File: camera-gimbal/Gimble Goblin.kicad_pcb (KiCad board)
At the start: 2 copper layers, 44.5 x 36.6 mm, 33 parts, among them J1 Conn_02x03_Odd_Even, J2 Conn_01x03_Male, J3 Conn_01x03_Male, J4 Conn_01x03_Male, J5 PROG, SW1 SW_Push, U1 L7805, U2 MCP2515-EST, U3 ATA6560,1, U4 L7805, U5 ATmega328P-AU, Y1 20MHz, Y2 16MHz

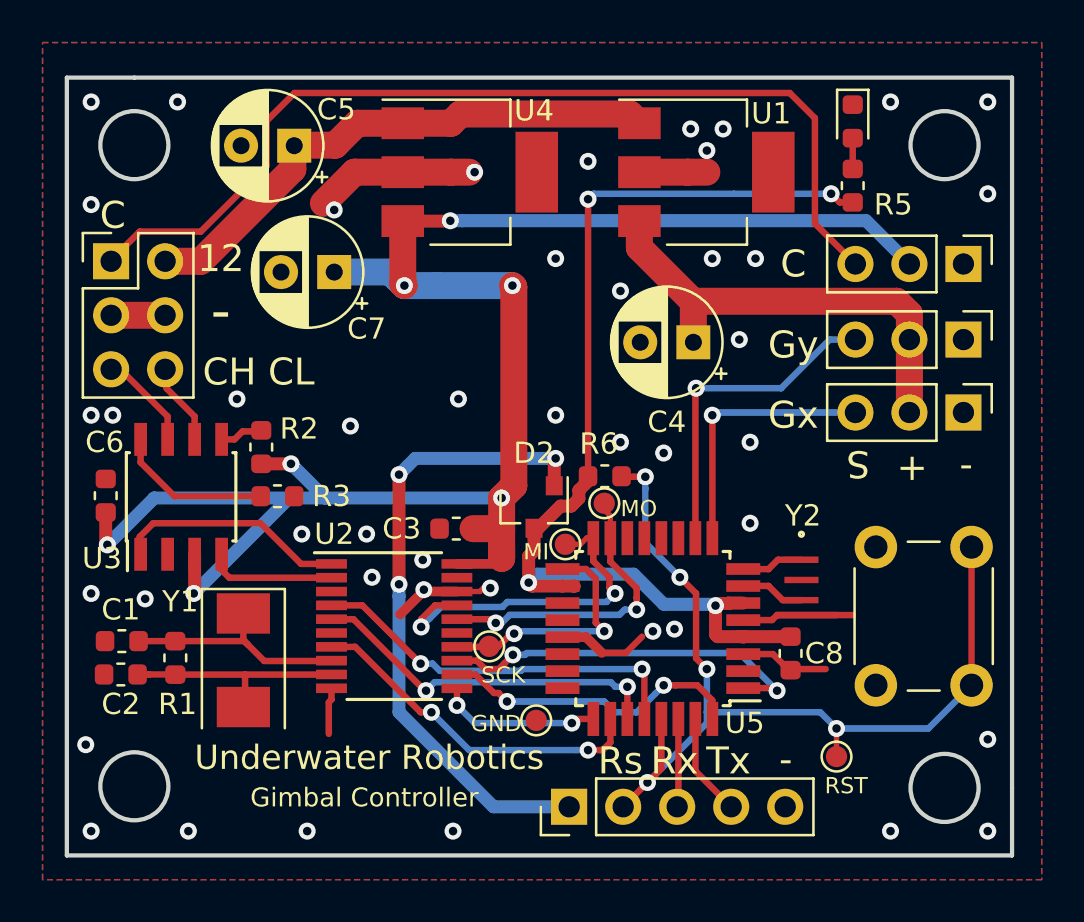
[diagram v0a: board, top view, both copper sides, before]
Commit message: Replaced moutning holes drawn in edge cuts with real holes and regenerated all gerbers
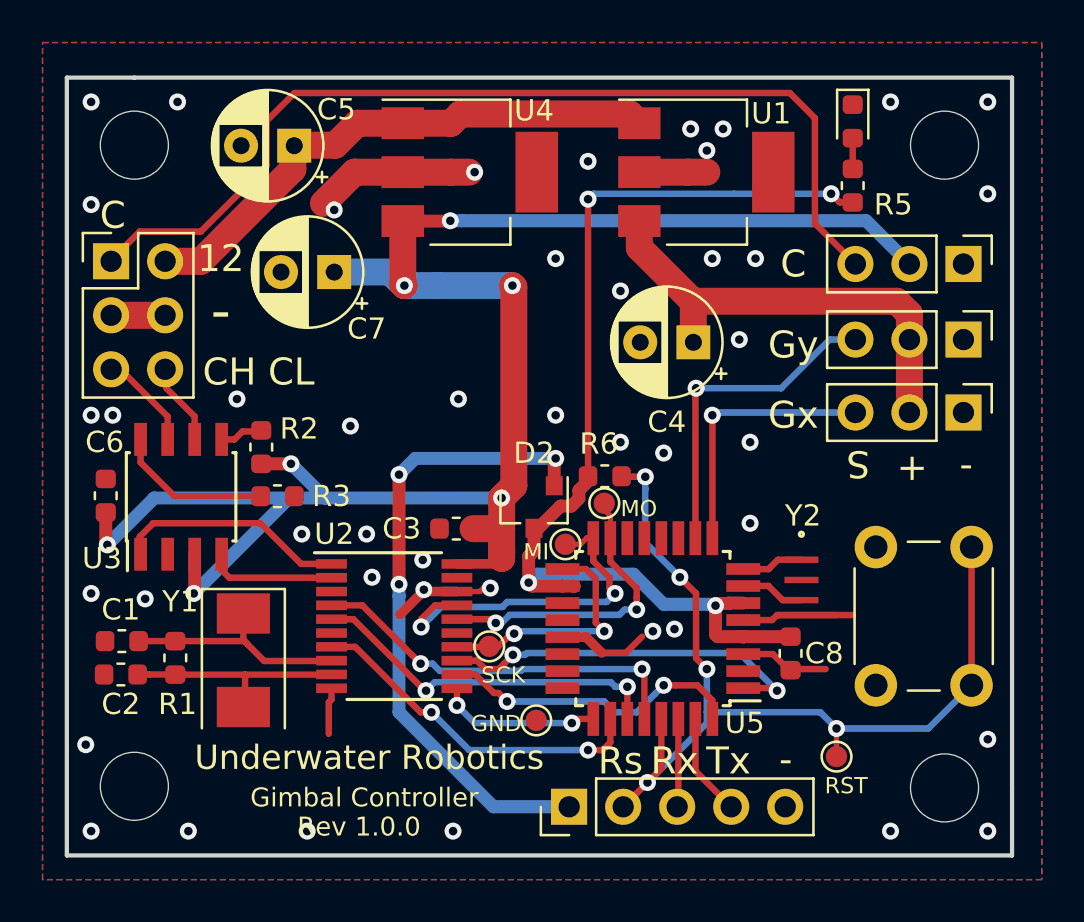
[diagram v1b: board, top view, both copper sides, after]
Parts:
- added REF**: MountingHole_3.2mm_M3, MountingHole:MountingHole_3.2mm_M3, F.Cu at (111.0, 98.5)
- added REF**: MountingHole_3.2mm_M3, MountingHole:MountingHole_3.2mm_M3, F.Cu at (149.1, 98.6)
- added REF**: MountingHole_3.2mm_M3, MountingHole:MountingHole_3.2mm_M3, F.Cu at (149.1, 68.3)
- added REF**: MountingHole_3.2mm_M3, MountingHole:MountingHole_3.2mm_M3, F.Cu at (111.0, 68.3)
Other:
- outline, holes or cut-outs redrawn
- board text added: "Rev 1.0.0"
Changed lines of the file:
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@@
   (general
     (thickness 1.6)
-    (drawings 31)
+    (drawings 28)
     (tracks 393)
     (zones 0)
-    (modules 33)
+    (modules 37)
     (nets 47)
   )
@@
       (drillshape 0)
       (scaleselection 1)
-      (outputdirectory "gerbers_drills/"))
+      (outputdirectory "C:/Users/User/Documents/GitHub/TITAN-Electrical/camera-gimbal/"))
   )
   (net 0 "")
@@
     (add_net VPP)
     (add_net V_MCU)
+  )
+  (module MountingHole:MountingHole_3.2mm_M3 (layer F.Cu)
+    (at 110.998 98.4758)
+    (descr "Mounting Hole 3.2mm, no annular, M3")
+    (tags "mounting hole 3.2mm no annular m3")
+    (attr virtual)
+    (fp_text reference REF** (at 0 -4.2) (layer F.SilkS) hide
+      (effects (font (size 1 1) (thickness 0.15)))
+    )
+    (fp_text value MountingHole_3.2mm_M3 (at 0 4.2) (layer F.Fab)
+      (effects (font (size 1 1) (thickness 0.15)))
+    )
+    (fp_text user %R (at 0.3 0) (layer F.Fab)
+      (effects (font (size 1 1) (thickness 0.15)))
+    )
+    (fp_circle (center 0 0) (end 3.2 0) (layer Cmts.User) (width 0.15))
+    (fp_circle (center 0 0) (end 3.45 0) (layer F.CrtYd) (width 0.05))
+    (pad 1 np_thru_hole circle (at 0 0) (size 3.2 3.2) (drill 3.2) (layers *.Cu *.Mask))
+  )
+  (module MountingHole:MountingHole_3.2mm_M3 (layer F.Cu)
+    (at 149.098 98.552)
+    (descr "Mounting Hole 3.2mm, no annular, M3")
+    (tags "mounting hole 3.2mm no annular m3")
+    (attr virtual)
+    (fp_text reference REF** (at 0 -4.2) (layer F.SilkS) hide
+      (effects (font (size 1 1) (thickness 0.15)))
+    )
+    (fp_text value MountingHole_3.2mm_M3 (at 0 4.2) (layer F.Fab)
+      (effects (font (size 1 1) (thickness 0.15)))
+    )
+    (fp_circle (center 0 0) (end 3.45 0) (layer F.CrtYd) (width 0.05))
+    (fp_circle (center 0 0) (end 3.2 0) (layer Cmts.User) (width 0.15))
+    (fp_text user %R (at 0.3 0) (layer F.Fab)
+      (effects (font (size 1 1) (thickness 0.15)))
+    )
+    (pad 1 np_thru_hole circle (at 0 0) (size 3.2 3.2) (drill 3.2) (layers *.Cu *.Mask))
+  )
+  (module MountingHole:MountingHole_3.2mm_M3 (layer F.Cu)
+    (at 149.098 68.326)
+    (descr "Mounting Hole 3.2mm, no annular, M3")
+    (tags "mounting hole 3.2mm no annular m3")
+    (attr virtual)
+    (fp_text reference REF** (at 0 -4.2) (layer F.SilkS) hide
+      (effects (font (size 1 1) (thickness 0.15)))
+    )
+    (fp_text value MountingHole_3.2mm_M3 (at 0 4.2) (layer F.Fab)
+      (effects (font (size 1 1) (thickness 0.15)))
+    )
+    (fp_text user %R (at 0.3 0) (layer F.Fab)
+      (effects (font (size 1 1) (thickness 0.15)))
+    )
+    (fp_circle (center 0 0) (end 3.2 0) (layer Cmts.User) (width 0.15))
+    (fp_circle (center 0 0) (end 3.45 0) (layer F.CrtYd) (width 0.05))
+    (pad 1 np_thru_hole circle (at 0 0) (size 3.2 3.2) (drill 3.2) (layers *.Cu *.Mask))
   )
   (module TestPoint:TestPoint_Pad_D1.0mm (layer F.Cu)
@@
     )
   )
+  (module MountingHole:MountingHole_3.2mm_M3 (layer F.Cu)
+    (at 110.998 68.326)
+    (descr "Mounting Hole 3.2mm, no annular, M3")
+    (tags "mounting hole 3.2mm no annular m3")
+    (attr virtual)
+    (fp_text reference REF** (at 0 -4.2) (layer F.SilkS) hide
+      (effects (font (size 1 1) (thickness 0.15)))
+    )
+    (fp_text value MountingHole_3.2mm_M3 (at 0 4.2) (layer F.Fab)
+      (effects (font (size 1 1) (thickness 0.15)))
+    )
+    (fp_circle (center 0 0) (end 3.45 0) (layer F.CrtYd) (width 0.05))
+    (fp_circle (center 0 0) (end 3.2 0) (layer Cmts.User) (width 0.15))
+    (fp_text user %R (at 0.3 0) (layer F.Fab)
+      (effects (font (size 1 1) (thickness 0.15)))
+    )
+    (pad 1 np_thru_hole circle (at 0 0) (size 3.2 3.2) (drill 3.2) (layers *.Cu *.Mask))
+  )
+  (gr_text "Rev 1.0.0" (at 121.5644 100.3808) (layer F.SilkS)
+    (effects (font (size 0.889 0.889) (thickness 0.22225)))
+  )
   (gr_text RST (at 144.4752 98.4504) (layer F.SilkS)
     (effects (font (size 0.762 0.762) (thickness 0.1905)))
@@
   (gr_line (start 152.273 65.151) (end 110.998 65.151) (layer Edge.Cuts) (width 0.2))
   (gr_line (start 110.998 65.151) (end 107.823 65.151) (layer Edge.Cuts) (width 0.2))
-  (gr_circle (center 149.098 98.552) (end 150.698 98.552) (layer Edge.Cuts) (width 0.2))
-  (gr_circle (center 110.998 98.476) (end 112.598 98.476) (layer Edge.Cuts) (width 0.2))
-  (gr_circle (center 149.098 68.326) (end 150.698 68.326) (layer Edge.Cuts) (width 0.2))
-  (gr_circle (center 110.998 68.326) (end 112.598 68.326) (layer Edge.Cuts) (width 0.2))
   (segment (start 123.621 72.023) (end 123.371 72.023) (width 1.27) (layer F.Cu) (net 1))
   (via (at 125.857 71.882) (size 0.8) (drill 0.4) (layers F.Cu B.Cu) (net 1))
